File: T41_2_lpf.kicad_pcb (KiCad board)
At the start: 2 copper layers, 100 x 100 mm, 116 parts, among them J1 5-1814832-1, J2 5-1814832-1, J3 5-1814832-1, J4 Conn_02x08_Odd_Even, J5 Conn_02x05_Odd_Even, J6 B2B-XH-A_LF__SN_, Q1 Q_NMOS_GSD, Q2 Q_NMOS_GSD, Q3 Q_NMOS_GSD, Q4 Q_NMOS_GSD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

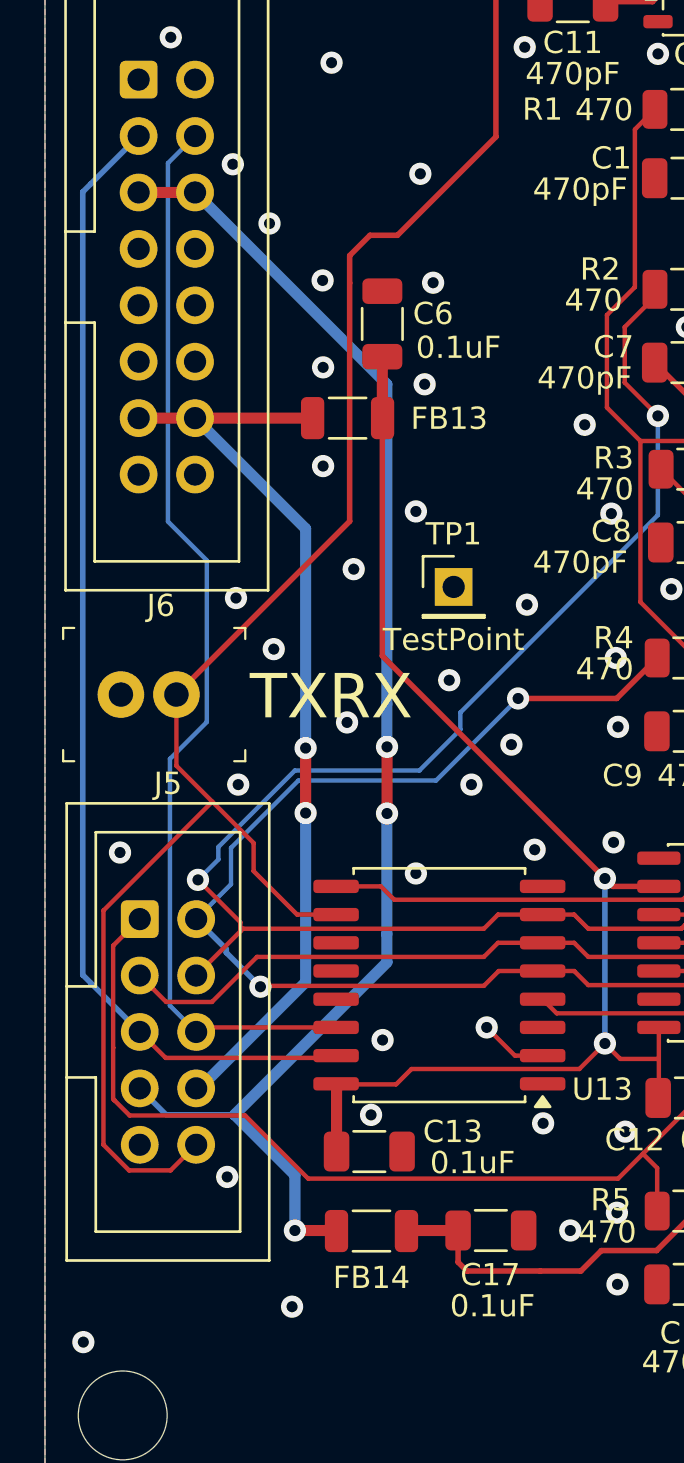
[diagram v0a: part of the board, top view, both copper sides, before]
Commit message: Had to make minor change to accomodate V10/V11 Main Board.
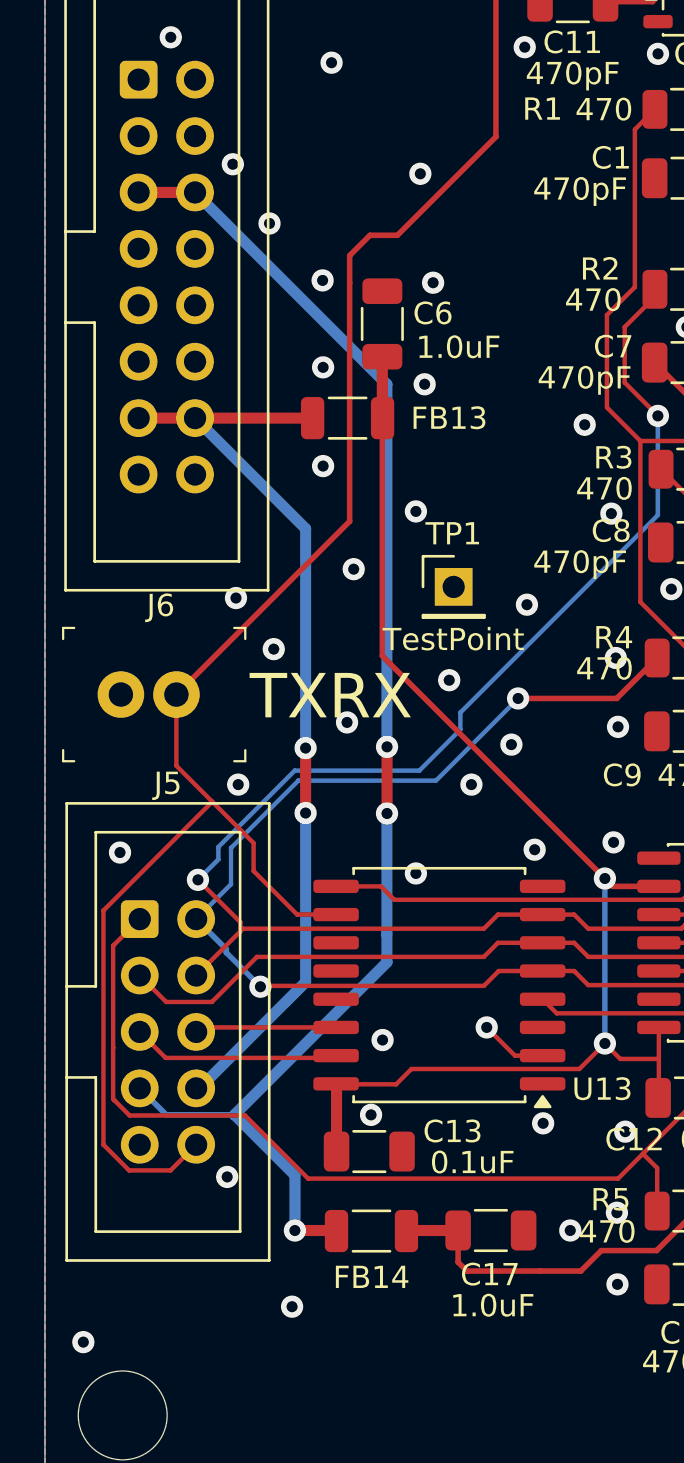
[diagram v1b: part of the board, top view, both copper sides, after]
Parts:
- C17, C6: value 0.1uF -> 1.0uF
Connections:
- J4 pad 3: /SDA -> unconnected-(J4-Pin_3-Pad3)
- J4 pad 4: /SCL -> unconnected-(J4-Pin_4-Pad4)
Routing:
- net /SCL: track 49.1 -> 6.38 mm
- net /SDA: track 52.7 -> 10.3 mm
